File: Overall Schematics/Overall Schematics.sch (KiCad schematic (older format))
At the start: 27 parts, among them J1 WattMeter1_Output, J2 WattMeter2_Output, J3 Intel_Buck_Converter_Input, J4 WattMeter1_Input, J5 WattMeter2_Input, M1 Stepper_Motor_bipolar, M2 Stepper_Motor_bipolar, M3 LinActuator12V, M4 LinActuator12V, M5 LinActuator12V, M6 Motor_DC, M7 Motor_DC, M8 Motor_DC, M9 Motor_DC, SW1 SW_DPST, U1 Teensy4.1, U10 VNH52019, U2 36v4SMD, U3 36v4SMD, U4 VNH52019, U5 VNH52019, U6 VNH52019, U7 VNH52019, U8 VNH52019, U9 VNH52019

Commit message: beginning of the pcb
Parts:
- BT1, BT2: footprint Custom Footprints:AMASS_XT60-M_1x02_P7.20mm_Vertical -> Custom Footprints:AMASS_XT60-F_1x02_P7.20mm_Vertical
- J1, J2, J3, J4, J5, M6, M7, M8, M9: footprint (none) -> TerminalBlock:TerminalBlock_bornier-2_P5.08mm
- M1, M2: footprint (none) -> TerminalBlock:TerminalBlock_bornier-4_P5.08mm
- M3, M4, M5: footprint (none) -> TerminalBlock:TerminalBlock_bornier-5_P5.08mm
- SW1: footprint (none) -> Button_Switch_SMD:SW_MEC_5GSH9
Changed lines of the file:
@@
 F 0 "M1" H 24738 10924 50  0000 L CNN
 F 1 "Stepper_Motor_bipolar" H 24738 10833 50  0000 L CNN
-F 2 "" H 24560 10790 50  0001 C CNN
+F 2 "TerminalBlock:TerminalBlock_bornier-4_P5.08mm" H 24560 10790 50  0001 C CNN
 F 3 "http://www.infineon.com/dgdl/Application-Note-TLE8110EE_driving_UniPolarStepperMotor_V1.1.pdf?fileId=db3a30431be39b97011be5d0aa0a00b0" H 24560 10790 50  0001 C CNN
 	1    24550 10800
@@
 F 0 "M2" H 24738 11974 50  0000 L CNN
 F 1 "Stepper_Motor_bipolar" H 24738 11883 50  0000 L CNN
-F 2 "" H 24560 11840 50  0001 C CNN
+F 2 "TerminalBlock:TerminalBlock_bornier-4_P5.08mm" H 24560 11840 50  0001 C CNN
 F 3 "http://www.infineon.com/dgdl/Application-Note-TLE8110EE_driving_UniPolarStepperMotor_V1.1.pdf?fileId=db3a30431be39b97011be5d0aa0a00b0" H 24560 11840 50  0001 C CNN
 	1    24550 11850
@@
 F 0 "M9" H 29858 10846 50  0000 L CNN
 F 1 "Motor_DC" H 29858 10755 50  0000 L CNN
-F 2 "" H 29700 10760 50  0001 C CNN
+F 2 "TerminalBlock:TerminalBlock_bornier-2_P5.08mm" H 29700 10760 50  0001 C CNN
 F 3 "~" H 29700 10760 50  0001 C CNN
 	1    29700 10850
@@
 F 0 "M6" H 29558 11596 50  0000 L CNN
 F 1 "Motor_DC" H 29558 11505 50  0000 L CNN
-F 2 "" H 29400 11510 50  0001 C CNN
+F 2 "TerminalBlock:TerminalBlock_bornier-2_P5.08mm" H 29400 11510 50  0001 C CNN
 F 3 "~" H 29400 11510 50  0001 C CNN
 	1    29400 11600
@@
 F 0 "M7" H 29558 12596 50  0000 L CNN
 F 1 "Motor_DC" H 29558 12505 50  0000 L CNN
-F 2 "" H 29400 12510 50  0001 C CNN
+F 2 "TerminalBlock:TerminalBlock_bornier-2_P5.08mm" H 29400 12510 50  0001 C CNN
 F 3 "~" H 29400 12510 50  0001 C CNN
 	1    29400 12600
@@
 Text GLabel 24650 11550 1    31   Input ~ 0
 AOUT2_2
-Text GLabel 24300 12450 1    31   Input ~ 0
-OUTA_1
 Text GLabel 29700 10650 1    31   Input ~ 0
 OUTA_2
@@
 F 0 "M5" H 25228 14322 20  0000 L CNN
 F 1 "LinActuator12V" H 25228 14279 20  0000 L CNN
-F 2 "" H 25350 14350 20  0001 C CNN
+F 2 "TerminalBlock:TerminalBlock_bornier-5_P5.08mm" H 25350 14350 20  0001 C CNN
 F 3 "" H 25350 14350 20  0001 C CNN
 	1    24950 14150
@@
 F 0 "M3" H 25178 15622 20  0000 L CNN
 F 1 "LinActuator12V" H 25178 15579 20  0000 L CNN
-F 2 "" H 25300 15650 20  0001 C CNN
+F 2 "TerminalBlock:TerminalBlock_bornier-5_P5.08mm" H 25300 15650 20  0001 C CNN
 F 3 "" H 25300 15650 20  0001 C CNN
 	1    24900 15450
@@
 F 0 "M4" H 25178 16972 20  0000 L CNN
 F 1 "LinActuator12V" H 25178 16929 20  0000 L CNN
-F 2 "" H 25300 17000 20  0001 C CNN
+F 2 "TerminalBlock:TerminalBlock_bornier-5_P5.08mm" H 25300 17000 20  0001 C CNN
 F 3 "" H 25300 17000 20  0001 C CNN
 	1    24900 16800
@@
 F 0 "BT1" V 27455 13850 50  0000 C CNN
 F 1 "True_Spec_Battery1" V 27546 13850 50  0000 C CNN
-F 2 "Custom Footprints:AMASS_XT60-M_1x02_P7.20mm_Vertical" V 27700 13910 50  0001 C CNN
+F 2 "Custom Footprints:AMASS_XT60-F_1x02_P7.20mm_Vertical" V 27700 13910 50  0001 C CNN
 F 3 "~" V 27700 13910 50  0001 C CNN
 	1    27700 13850
@@
 F 0 "SW1" H 28700 14475 50  0000 C CNN
 F 1 "SW_DPST" H 28700 14384 50  0000 C CNN
-F 2 "" H 28700 14150 50  0001 C CNN
+F 2 "Button_Switch_SMD:SW_MEC_5GSH9" H 28700 14150 50  0001 C CNN
 F 3 "~" H 28700 14150 50  0001 C CNN
 	1    28700 14150
@@
 F 0 "BT2" V 27455 14250 50  0000 C CNN
 F 1 "True_Spec_Battery2" V 27546 14250 50  0000 C CNN
-F 2 "Custom Footprints:AMASS_XT60-M_1x02_P7.20mm_Vertical" V 27700 14310 50  0001 C CNN
+F 2 "Custom Footprints:AMASS_XT60-F_1x02_P7.20mm_Vertical" V 27700 14310 50  0001 C CNN
 F 3 "~" V 27700 14310 50  0001 C CNN
 	1    27700 14250
@@
 F 0 "J4" H 29530 13842 50  0000 L CNN
 F 1 "WattMeter1_Input" H 29530 13751 50  0000 L CNN
-F 2 "" H 29450 13850 50  0001 C CNN
+F 2 "TerminalBlock:TerminalBlock_bornier-2_P5.08mm" H 29450 13850 50  0001 C CNN
 F 3 "~" H 29450 13850 50  0001 C CNN
 	1    29450 13850
@@
 F 0 "J5" H 29530 14292 50  0000 L CNN
 F 1 "WattMeter2_Input" H 29530 14201 50  0000 L CNN
-F 2 "" H 29450 14300 50  0001 C CNN
+F 2 "TerminalBlock:TerminalBlock_bornier-2_P5.08mm" H 29450 14300 50  0001 C CNN
 F 3 "~" H 29450 14300 50  0001 C CNN
 	1    29450 14300
@@
 F 0 "J1" H 27118 14575 50  0000 C CNN
 F 1 "WattMeter1_Output" H 27118 14666 50  0000 C CNN
-F 2 "" H 27200 14900 50  0001 C CNN
+F 2 "TerminalBlock:TerminalBlock_bornier-2_P5.08mm" H 27200 14900 50  0001 C CNN
 F 3 "~" H 27200 14900 50  0001 C CNN
 	1    27200 14900
@@
 F 0 "J2" H 27118 15025 50  0000 C CNN
 F 1 "WattMeter2_Output" H 27118 15116 50  0000 C CNN
-F 2 "" H 27200 15350 50  0001 C CNN
+F 2 "TerminalBlock:TerminalBlock_bornier-2_P5.08mm" H 27200 15350 50  0001 C CNN
 F 3 "~" H 27200 15350 50  0001 C CNN
 	1    27200 15350
@@
 F 0 "J3" H 29230 14792 50  0000 L CNN
 F 1 "Intel_Buck_Converter_Input" H 29230 14701 50  0000 L CNN
-F 2 "" H 29150 14800 50  0001 C CNN
+F 2 "TerminalBlock:TerminalBlock_bornier-2_P5.08mm" H 29150 14800 50  0001 C CNN
 F 3 "~" H 29150 14800 50  0001 C CNN
 	1    29150 14800
@@
 F 0 "M8" H 29658 9846 50  0000 L CNN
 F 1 "Motor_DC" H 29658 9755 50  0000 L CNN
-F 2 "" H 29500 9760 50  0001 C CNN
+F 2 "TerminalBlock:TerminalBlock_bornier-2_P5.08mm" H 29500 9760 50  0001 C CNN
 F 3 "~" H 29500 9760 50  0001 C CNN
 	1    29500 9850

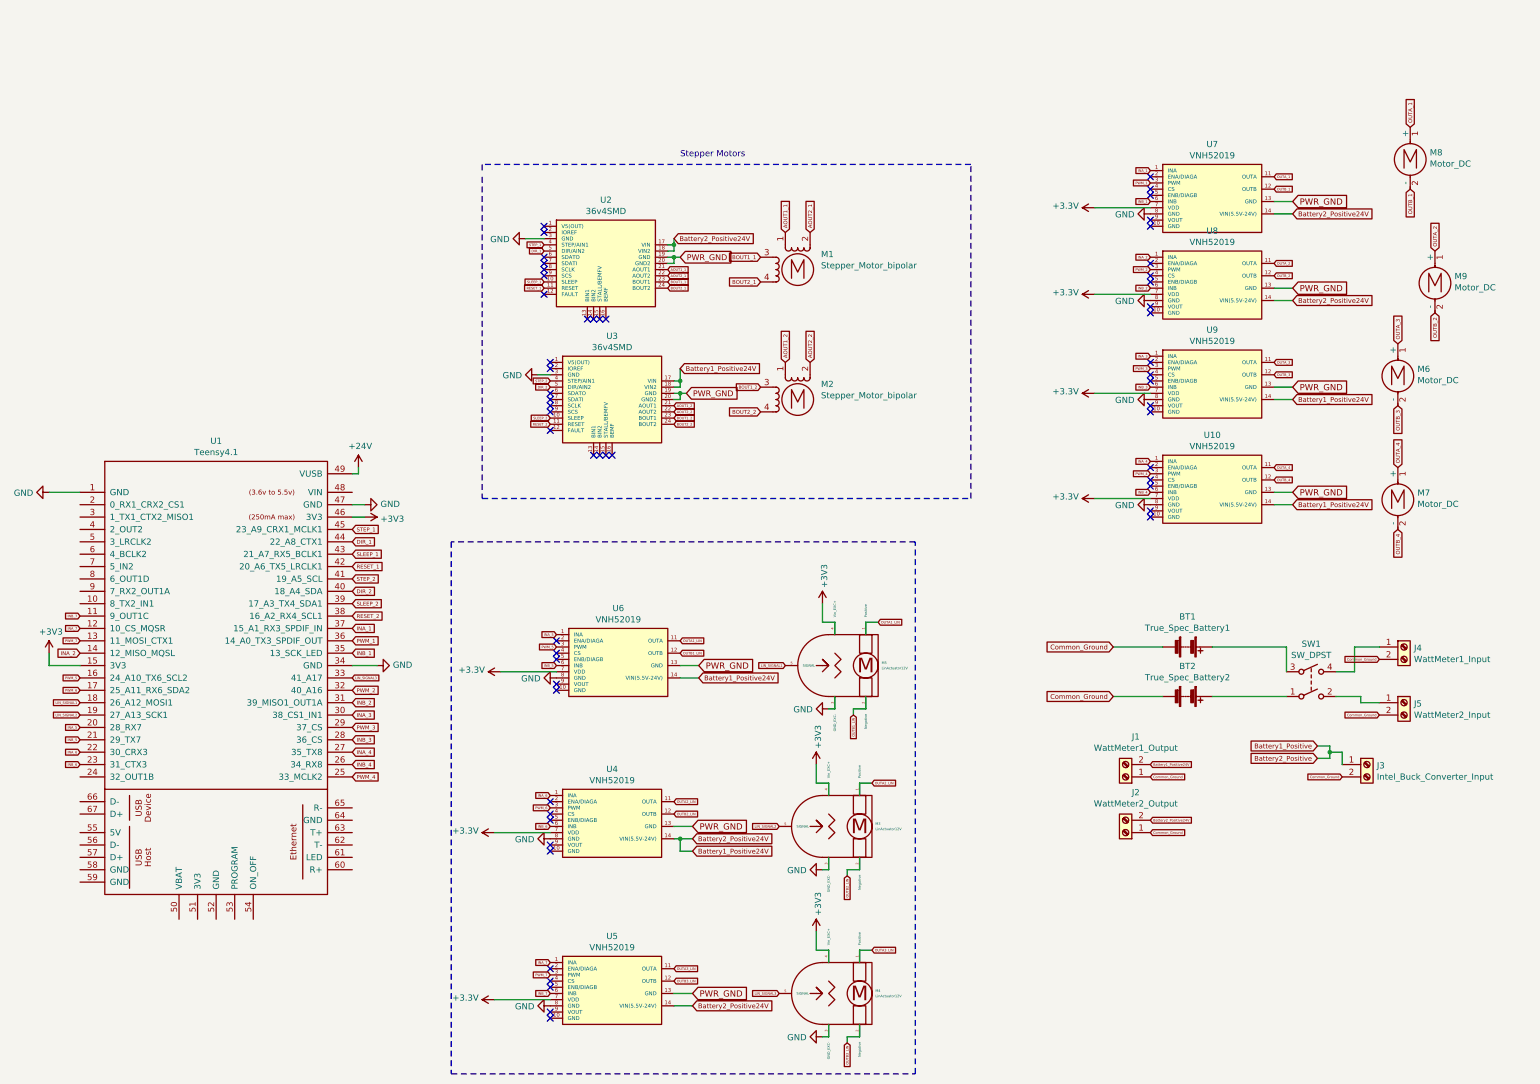
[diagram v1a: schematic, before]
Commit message: started PCB traces, need to add maestro servo board stuff
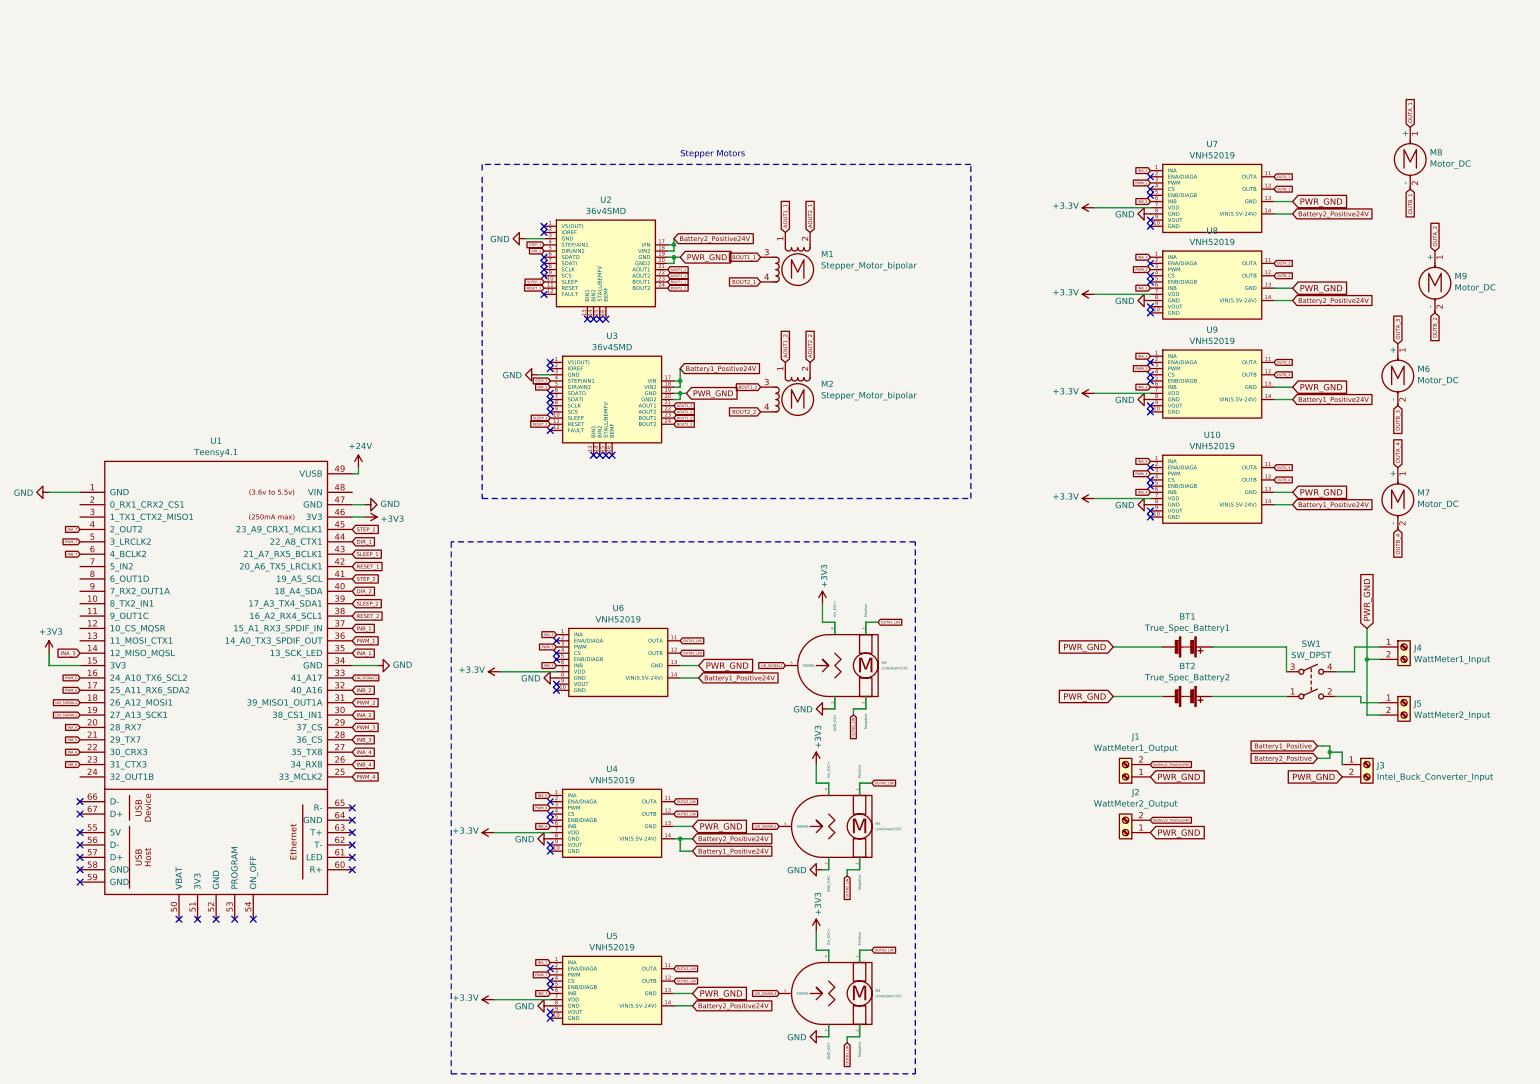
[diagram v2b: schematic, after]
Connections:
- net Common_Ground is gone; now on net PWR_GND: BT1.2 (-), BT2.2 (-), J1.1 (Pin_1), J2.1 (Pin_1), J3.2 (Pin_2), J4.2 (Pin_2), J5.2 (Pin_2)
- net INA_1: now also U1.35 (13_SCK_LED); no longer U1.37 (15_A1_RX3_SPDIF_IN)
- net INA_2: now also U1.30 (38_CS1_IN1); no longer U1.14 (12_MISO_MQSL)
- net INA_3: now also U1.14 (12_MISO_MQSL); no longer U1.30 (38_CS1_IN1)
- net INA_7: now also U1.4 (2_OUT2); no longer U1.12 (10_CS_MQSR)
- net INB_1: now also U1.37 (15_A1_RX3_SPDIF_IN); no longer U1.35 (13_SCK_LED)
- net INB_2: now also U1.32 (40_A16); no longer U1.31 (39_MISO1_OUT1A)
- net INB_7: now also U1.6 (4_BCLK2); no longer U1.11 (9_OUT1C)
- net PWM_2: now also U1.31 (39_MISO1_OUT1A); no longer U1.32 (40_A16)
- net PWM_7: now also U1.5 (3_LRCLK2); no longer U1.13 (11_MOSI_CTX1)
- no-connect marks 57 -> 75
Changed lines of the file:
@@
 Text GLabel 20950 13600 2    31   Input ~ 0
 RESET_2
-Text GLabel 20950 13700 2    31   Input ~ 0
+Text GLabel 20950 13900 2    31   Input ~ 0
 INA_1
 Text GLabel 20950 13800 2    31   Input ~ 0
 PWM_1
-Text GLabel 20950 13900 2    31   Input ~ 0
+Text GLabel 20950 13700 2    31   Input ~ 0
 INB_1
+Text GLabel 20950 14400 2    31   Input ~ 0
+INA_2
+Text GLabel 20950 14300 2    31   Input ~ 0
+PWM_2
+Text GLabel 20950 14200 2    31   Input ~ 0
+INB_2
 Text GLabel 18750 13900 0    31   Input ~ 0
-INA_2
-Text GLabel 20950 14200 2    31   Input ~ 0
-PWM_2
-Text GLabel 20950 14300 2    31   Input ~ 0
-INB_2
-Text GLabel 20950 14400 2    31   Input ~ 0
 INA_3
 Text GLabel 20950 14600 2    31   Input ~ 0
@@
 Text GLabel 24400 16650 0    20   Input ~ 0
 LIN_SIGNAL3
-Text GLabel 18750 13700 0    20   Input ~ 0
+Text GLabel 18750 12900 0    20   Input ~ 0
 INA_7
-Text GLabel 18750 13800 0    20   Input ~ 0
+Text GLabel 18750 13000 0    20   Input ~ 0
 PWM_7
-Text GLabel 18750 13600 0    20   Input ~ 0
+Text GLabel 18750 13100 0    20   Input ~ 0
 INB_7
 Text GLabel 20950 14100 2    20   Input ~ 0
@@
 Wire Wire Line
 	27500 14250 27100 14250
-Text GLabel 27100 14250 0    39   Input ~ 0
-Common_Ground
-Text GLabel 27100 13850 0    39   Input ~ 0
-Common_Ground
-Text GLabel 29250 14400 0    20   Input ~ 0
-Common_Ground
-Text GLabel 27400 15350 2    20   Input ~ 0
-Common_Ground
-Text GLabel 27400 14900 2    20   Input ~ 0
-Common_Ground
 $Comp
 L Connector:Screw_Terminal_01x02 J3
@@
 	1    0    0    -1
 $EndComp
-Text GLabel 28950 14900 0    20   Input ~ 0
-Common_Ground
 Text GLabel 27400 14800 2    20   Input ~ 0
 Battery1_Positive24V
@@
 Text GLabel 23700 16750 2    39   Input ~ 0
 Battery2_Positive24V
-Text GLabel 29250 13950 0    20   Input ~ 0
-Common_Ground
 Text GLabel 23700 15400 2    39   Input ~ 0
 Battery2_Positive24V
@@
 	1    0    0    -1
 $EndComp
+NoConn ~ 20950 15150
+NoConn ~ 20950 15250
+NoConn ~ 20950 15350
+NoConn ~ 20950 15450
+NoConn ~ 20950 15550
+NoConn ~ 20950 15650
+NoConn ~ 20150 16050
+NoConn ~ 20000 16050
+NoConn ~ 19850 16050
+NoConn ~ 19700 16050
+NoConn ~ 19550 16050
+NoConn ~ 18750 15750
+NoConn ~ 18750 15650
+NoConn ~ 18750 15550
+NoConn ~ 18750 15450
+NoConn ~ 18750 15350
+NoConn ~ 18750 15200
+NoConn ~ 18750 15100
+Text GLabel 27100 13850 0    50   Input ~ 0
+PWR_GND
+Text GLabel 27100 14250 0    50   Input ~ 0
+PWR_GND
+Text GLabel 29150 13700 1    50   Input ~ 0
+PWR_GND
+Wire Wire Line
+	29250 13950 29150 13950
+Wire Wire Line
+	29150 13950 29150 13700
+Wire Wire Line
+	29150 13950 29150 14400
+Wire Wire Line
+	29150 14400 29250 14400
+Connection ~ 29150 13950
+Text GLabel 28950 14900 0    50   Input ~ 0
+PWR_GND
+Text GLabel 27400 14900 2    50   Input ~ 0
+PWR_GND
+Text GLabel 27400 15350 2    50   Input ~ 0
+PWR_GND
 $EndSCHEMATC

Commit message: new symbol
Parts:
- added M?: Stepper_Motor_bipolar, TerminalBlock:TerminalBlock_bornier-4_P5.08mm, symbol Motor:Stepper_Motor_bipolar
- added M?: Motor_Servo, symbol Motor:Motor_Servo
- added U?: 36v4SMD, symbol CustomLibrary:36v4SMD
- added U?: ServoDriver, symbol CustomLibrary:ServoDriver
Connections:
- net Battery1_Positive24V: now also U?.17 (VIN), U?.18 (VIN2)
- net GND: now also U?.3 (GND)
- net PWR_GND: now also U?.19 (GND), U?.20 (GND2)
- net STEP_3: now reaches U1.10 (8_TX2_IN1)
- net STEP_3: now also U?.4 (STEP/AIN1)
- net DIR_3: now reaches U1.11 (9_OUT1C)
- net DIR_3: now also U?.5 (DIR/AIN2)
- net SLEEP_3: now reaches U1.12 (10_CS_MQSR)
- net SLEEP_3: now also U?.10 (SLEEP)
- net RESET_3: now reaches U1.13 (11_MOSI_CTX1)
- net RESET_3: now also U?.11 (RESET)
- new net: M?.1 (PWM), U?.1 (Signal_1)
- new net: M?.3 (-), U?.13 (-_1)
- new net: M?.2 (+), U?.7 (+_1)
- new net AOUT1_3: M?.1, U?.21 (AOUT1)
- new net AOUT2_3: M?.2 (-), U?.22 (AOUT2)
- new net BOUT1_3: M?.3, U?.23 (BOUT1)
- new net BOUT2_3: M?.4, U?.24 (BOUT2)
- no-connect marks 75 -> 101
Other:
- note removed: "Stepper Motors"
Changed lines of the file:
@@
 OUTB_4
 Wire Notes Line
-	22000 10050 22000 12650
-Wire Notes Line
 	22000 12650 25950 12650
-Wire Notes Line
-	25950 12650 25950 9950
-Wire Notes Line
-	25950 9950 22000 9950
-Wire Notes Line
-	22000 9950 22000 10000
-Text Notes 23600 9900 0    50   ~ 0
-Stepper Motors
 Wire Wire Line
 	24850 14350 24800 14350
@@
 	21750 13000 21750 17300
 Wire Notes Line
-	21750 17300 25500 17300
-Wire Notes Line
 	25500 17300 25500 13000
 Wire Notes Line
@@
 Text GLabel 27400 15350 2    50   Input ~ 0
 PWR_GND
+Wire Notes Line
+	21750 17300 25500 17300
+$Comp
+L CustomLibrary:36v4SMD U?
+U 1 1 6009DFB5
+P 23000 9200
+F 0 "U?" H 23000 9263 50  0000 C CNN
+F 1 "36v4SMD" H 23000 9172 50  0000 C CNN
+F 2 "" H 23000 9200 50  0001 C CNN
+F 3 "" H 23000 9200 50  0001 C CNN
+	1    23000 9200
+	1    0    0    -1
+$EndComp
+NoConn ~ 22500 9350
+NoConn ~ 22500 9400
+NoConn ~ 22500 9600
+NoConn ~ 22500 9650
+NoConn ~ 22500 9700
+NoConn ~ 22500 9750
+NoConn ~ 22500 9900
+NoConn ~ 22850 10100
+NoConn ~ 22900 10100
+NoConn ~ 22950 10100
+NoConn ~ 23000 10100
+$Comp
+L power:GND #PWR?
+U 1 1 600BE28C
+P 22350 9450
+F 0 "#PWR?" H 22350 9200 50  0001 C CNN
+F 1 "GND" V 22355 9322 50  0000 R CNN
+F 2 "" H 22350 9450 50  0001 C CNN
+F 3 "" H 22350 9450 50  0001 C CNN
+	1    22350 9450
+	0    1    1    0
+$EndComp
+Wire Wire Line
+	22350 9450 22500 9450
+Text GLabel 22500 9500 0    20   Input ~ 0
+STEP_3
+Text GLabel 22500 9550 0    20   Input ~ 0
+DIR_3
+Text GLabel 22500 9800 0    20   Input ~ 0
+SLEEP_3
+Text GLabel 22500 9850 0    20   Input ~ 0
+RESET_3
+$Comp
+L Motor:Stepper_Motor_bipolar M?
+U 1 1 600C6332
+P 24450 9650
+F 0 "M?" H 24638 9774 50  0000 L CNN
+F 1 "Stepper_Motor_bipolar" H 24638 9683 50  0000 L CNN
+F 2 "TerminalBlock:TerminalBlock_bornier-4_P5.08mm" H 24460 9640 50  0001 C CNN
+F 3 "http://www.infineon.com/dgdl/Application-Note-TLE8110EE_driving_UniPolarStepperMotor_V1.1.pdf?fileId=db3a30431be39b97011be5d0aa0a00b0" H 24460 9640 50  0001 C CNN
+	1    24450 9650
+	1    0    0    -1
+$EndComp
+Text GLabel 24150 9550 0    31   Input ~ 0
+BOUT1_3
+Text GLabel 24150 9750 0    31   Input ~ 0
+BOUT2_3
+Text GLabel 24350 9350 1    31   Input ~ 0
+AOUT1_3
+Text GLabel 24550 9350 1    31   Input ~ 0
+AOUT2_3
+Wire Wire Line
+	23500 9550 23600 9550
+Wire Wire Line
+	23600 9550 23600 9500
+Wire Wire Line
+	23500 9500 23600 9500
+Connection ~ 23600 9500
+Wire Wire Line
+	23600 9500 23600 9450
+Text GLabel 23600 9450 2    20   Input ~ 0
+Battery2_Positive24V
+Text GLabel 23600 9600 2    20   Input ~ 0
+PWR_GND
+Wire Wire Line
+	23500 9650 23550 9650
+Wire Wire Line
+	23550 9650 23550 9600
+Wire Wire Line
+	23500 9600 23550 9600
+Connection ~ 23550 9600
+Wire Wire Line
+	23550 9600 23600 9600
+Text GLabel 23500 9700 2    20   Input ~ 0
+AOUT1_3
+Text GLabel 23500 9750 2    20   Input ~ 0
+AOUT2_3
+Text GLabel 23500 9800 2    20   Input ~ 0
+BOUT1_3
+Text GLabel 23500 9850 2    20   Input ~ 0
+BOUT2_3
+Wire Notes Line
+	25950 8700 22000 8700
+Wire Notes Line
+	25950 8700 25950 12650
+Wire Notes Line
+	22000 8700 22000 12650
+Wire Notes Line
+	26450 13200 30300 13200
+Wire Notes Line
+	30300 9250 26450 9250
+Wire Notes Line
+	26450 15450 30300 15450
+Wire Notes Line
+	26450 9250 26450 15450
+Wire Notes Line
+	30300 9250 30300 15450
+Text GLabel 18750 13800 0    20   Input ~ 0
+RESET_3
+Text GLabel 18750 13700 0    20   Input ~ 0
+SLEEP_3
+Text GLabel 18750 13600 0    20   Input ~ 0
+DIR_3
+Text GLabel 18750 13500 0    20   Input ~ 0
+STEP_3
+$Comp
+L CustomLibrary:ServoDriver U?
+U 1 1 6010875A
+P 19450 10500
+F 0 "U?" H 19475 10543 20  0000 C CNN
+F 1 "ServoDriver" H 19475 10500 20  0000 C CNN
+F 2 "" H 19450 10600 20  0001 C CNN
+F 3 "" H 19450 10600 20  0001 C CNN
+	1    19450 10500
+	1    0    0    -1
+$EndComp
+$Comp
+L Motor:Motor_Servo M?
+U 1 1 601479AE
+P 20450 10700
+F 0 "M?" H 20782 10765 50  0000 L CNN
+F 1 "Motor_Servo" H 20782 10674 50  0000 L CNN
+F 2 "" H 20450 10510 50  0001 C CNN
+F 3 "http://forums.parallax.com/uploads/attachments/46831/74481.png" H 20450 10510 50  0001 C CNN
+	1    20450 10700
+	1    0    0    -1
+$EndComp
+Wire Wire Line
+	19800 10600 20150 10600
+Wire Wire Line
+	19650 11050 19650 11100
+Wire Wire Line
+	19650 11100 20050 11100
+Wire Wire Line
+	20050 11100 20050 10700
+Wire Wire Line
+	20050 10700 20150 10700
+Wire Wire Line
+	19150 10900 19100 10900
+Wire Wire Line
+	19100 10900 19100 11150
+Wire Wire Line
+	19100 11150 20100 11150
+Wire Wire Line
+	20100 11150 20100 10800
+Wire Wire Line
+	20100 10800 20150 10800
+NoConn ~ 19800 10650
+NoConn ~ 19800 10700
+NoConn ~ 19800 10750
+NoConn ~ 19800 10800
+NoConn ~ 19800 10850
+NoConn ~ 19600 11050
+NoConn ~ 19550 11050
+NoConn ~ 19500 11050
+NoConn ~ 19450 11050
+NoConn ~ 19400 11050
+NoConn ~ 19150 10850
+NoConn ~ 19150 10800
+NoConn ~ 19150 10750
+NoConn ~ 19150 10700
+NoConn ~ 19150 10650
+Wire Notes Line
+	18900 10250 21300 10250
+Wire Notes Line
+	21300 10250 21300 11250
+Wire Notes Line
+	21300 11250 18900 11250
+Wire Notes Line
+	18900 11250 18900 10250
 $EndSCHEMATC
